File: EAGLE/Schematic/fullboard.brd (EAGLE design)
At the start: 130.2 x 79.7 mm, 77 parts, among them CN1 B4B-XH-A, CN2 B4B-XH-A, IC1 IFX007T, IC2 IFX007T, IC3 IFX007T, IC4 IFX007T, J1 10118193-0001LF, Q1 8MHz ±10ppm Crystal 18pF 80 O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, SW1 TR1-SPST, U1 ATXMEGA128A3U-AU, U2 FT232RL-REEL

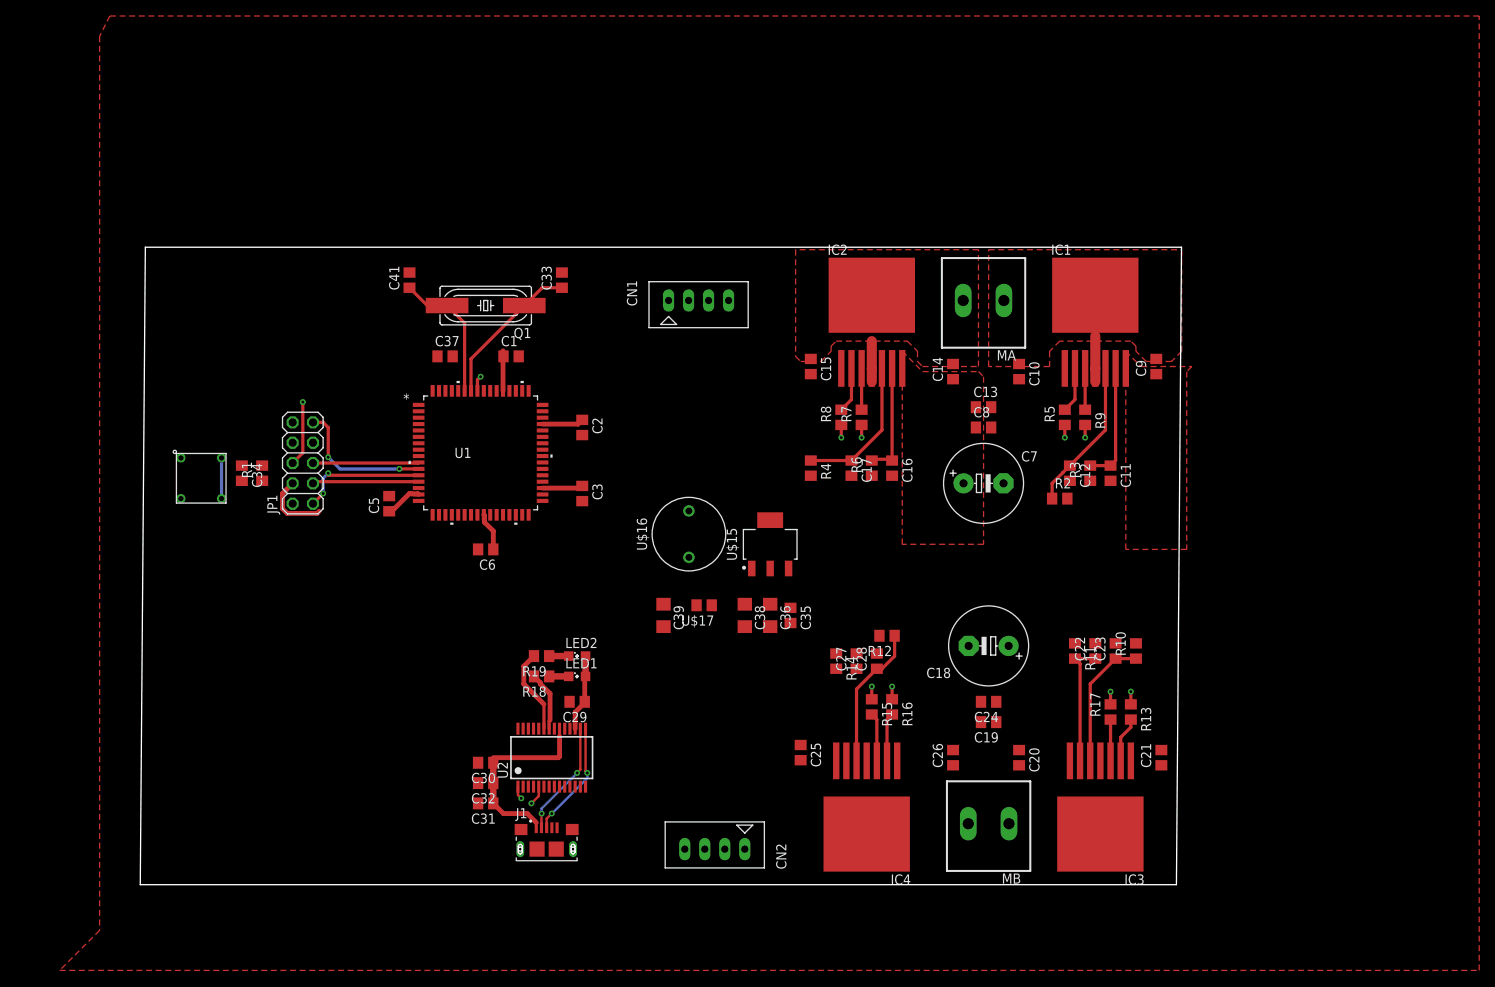
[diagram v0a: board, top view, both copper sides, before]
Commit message: V0.1 of the board
Did some more signal routing, added a connector for the mouse, added a simple 5V regulator circuit
Still need:
* Edge sensor connectors
* Footprint 2x check
* Probably some other things
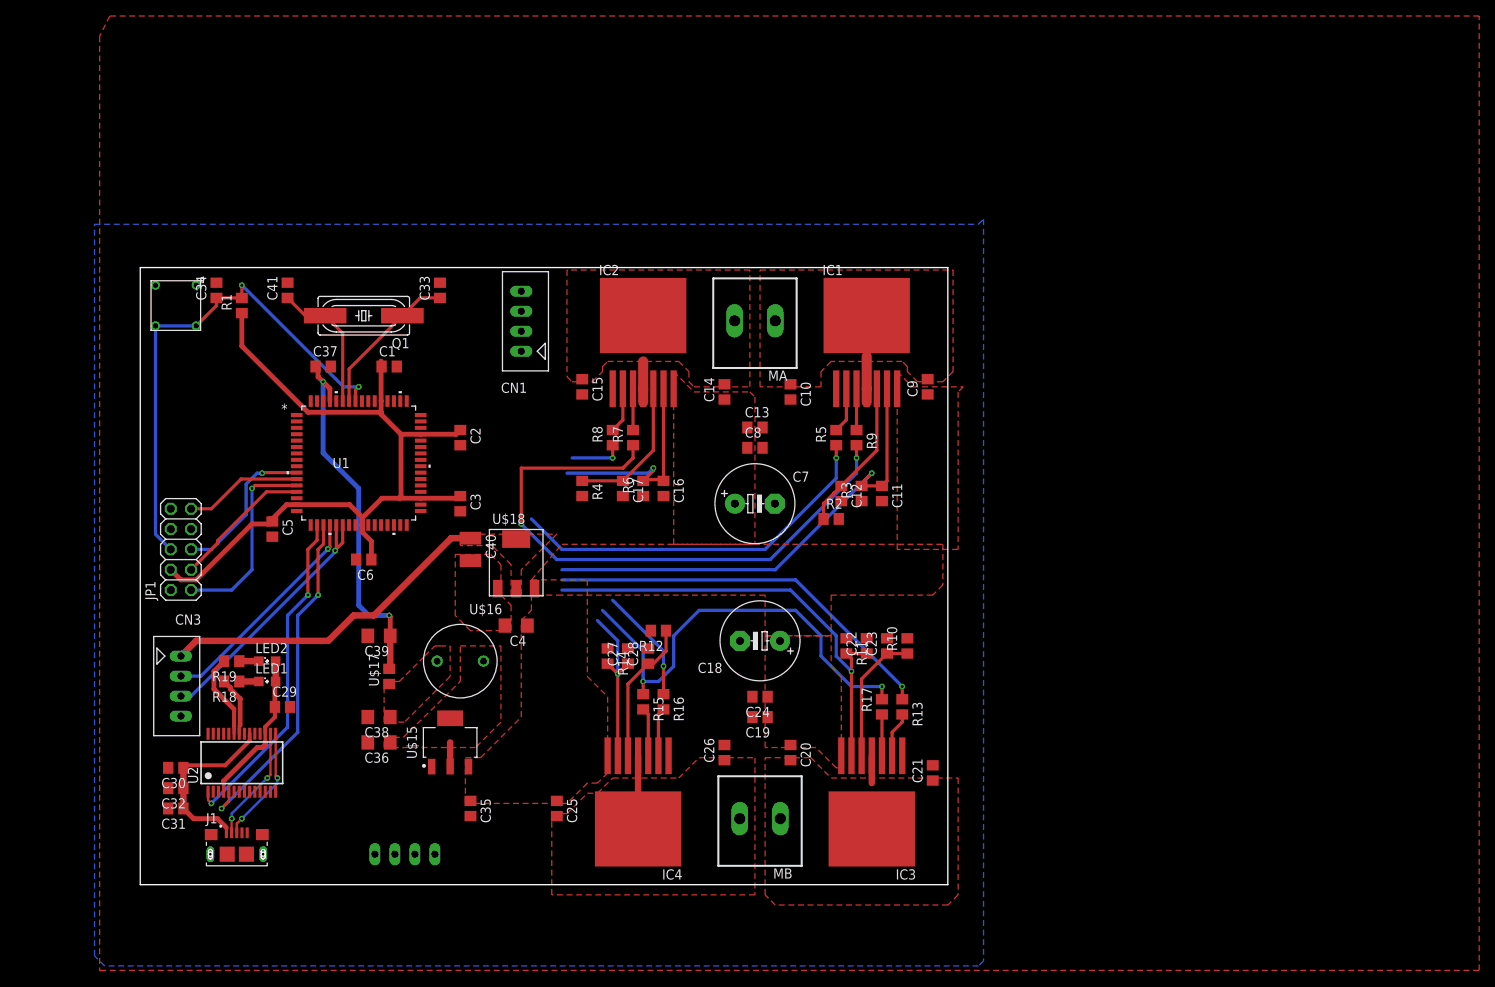
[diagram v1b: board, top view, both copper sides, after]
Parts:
- added C4: 10uF, rcl:C1206
- added C40: 22uF, rcl:C1210
- added CN3: B4B-XH-A, jst:B4B-XH-A
- added U$18: AZ1117IH, SumBot:SOT223
- moved C36 51.4 mm to (29.8, 18.4), turned to 180 degrees
- moved C38 47.5 mm to (29.8, 21.6), turned to 180 degrees
- moved U$15 47.1 mm to (38.7, 18.4)
- moved C35 46.7 mm to (41.3, 10.2)
- moved U$17 40.4 mm to (31.1, 26.7), turned to 90 degrees
- moved C30 38.7 mm to (4.45, 15.2)
- moved C31 38.7 mm to (4.45, 10.2)
- moved C32 38.7 mm to (4.45, 12.7)
- moved CN2 38.7 mm to (36.8, 4.45), flipped to the bottom, turned to 180 degrees
- moved J1 38.7 mm to (12.1, 4.45)
- moved LED1 38.7 mm to (15.9, 26.0)
- moved LED2 38.7 mm to (15.9, 28.6)
- moved R18 38.7 mm to (11.4, 26.0)
- moved R19 38.7 mm to (11.4, 28.6)
- moved U2 38.7 mm to (12.7, 15.9)
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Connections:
- net N$36 renamed VCCIO
- removed net RX_MSE: U1.21
- removed net TX_MSE: U1.22
- new net N$1: C4.2, C40.2, U$18.1
- new net TX/RX_MSE: CN3.3, U1.21, U1.22
- new net USB_PWR: C30.1, C31.1, C32.1, J1.1, U2.20
- net +12V: now also C4.1, U$18.3
- net +5V: now also C40.1, CN3.1, U$18.2, U$18.4; no longer C30.1, C31.1, C32.1, J1.1, U2.20
- net GND: now also CN3.4
- net XCK_MSE: now also CN3.2
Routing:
- net EN_A: track 3.18 -> 74.8 mm
- net +3V3: track 33.4 -> 99.9 mm
- net CS_B: track 15.6 -> 79.0 mm, vias 0 -> 2
- net CS_A: track 29.8 -> 88.8 mm, vias 0 -> 2
- net EN_B: track 3.18 -> 55.4 mm
- net !RESET: track 15.2 -> 64.9 mm
- net FWD_B: track 1.59 -> 49.7 mm
- net AVCC: track 0.00 -> 46.0 mm, vias 0 -> 2
- net FWD_A: track 1.59 -> 47.5 mm
- net TX_FT232: track 2.47 -> 43.2 mm, vias 1 -> 2
- net RX_FT232: track 1.63 -> 41.9 mm, vias 1 -> 2
- net TX/RX_MSE: track 0.00 -> 33.5 mm, vias 0 -> 1
- net XCK_MSE: track 0.00 -> 28.1 mm, vias 0 -> 1
- net USB_PWR: track 0.00 -> 22.2 mm
- net +5V: track 22.6 -> 42.3 mm
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- added copper zone on layer 1, net +3V3
- added copper zone on layer 1, net +5V
- added copper zone on layer 16, net GND
- added copper zone on layer 1, net MB_1
- added copper zone on layer 1, net MB_2
- added copper zone on layer 1, net N$1
- added copper zone on layer 1, net N$8
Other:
- board size 130.2 x 79.7 mm -> 100.9 x 77.1 mm

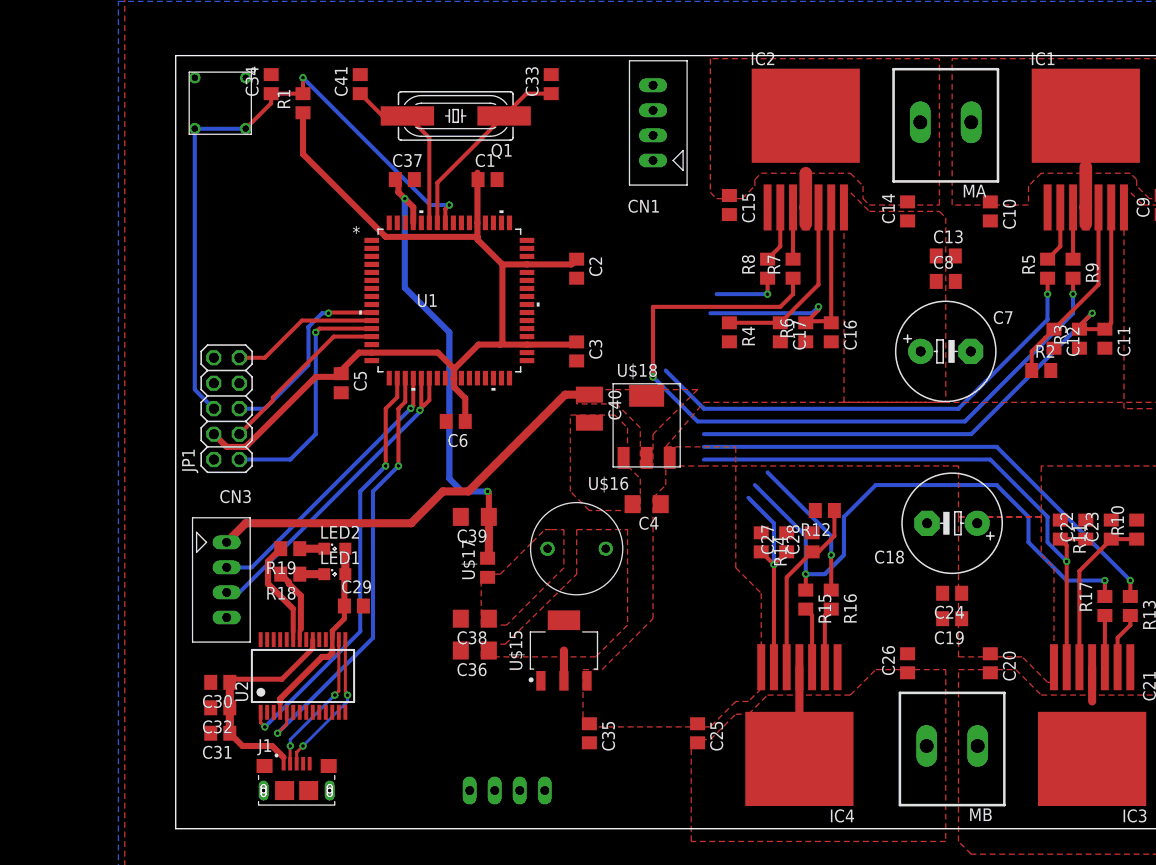
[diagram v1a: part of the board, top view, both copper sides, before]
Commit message: V0.2
Added Edge Detection and reconfigured other pins
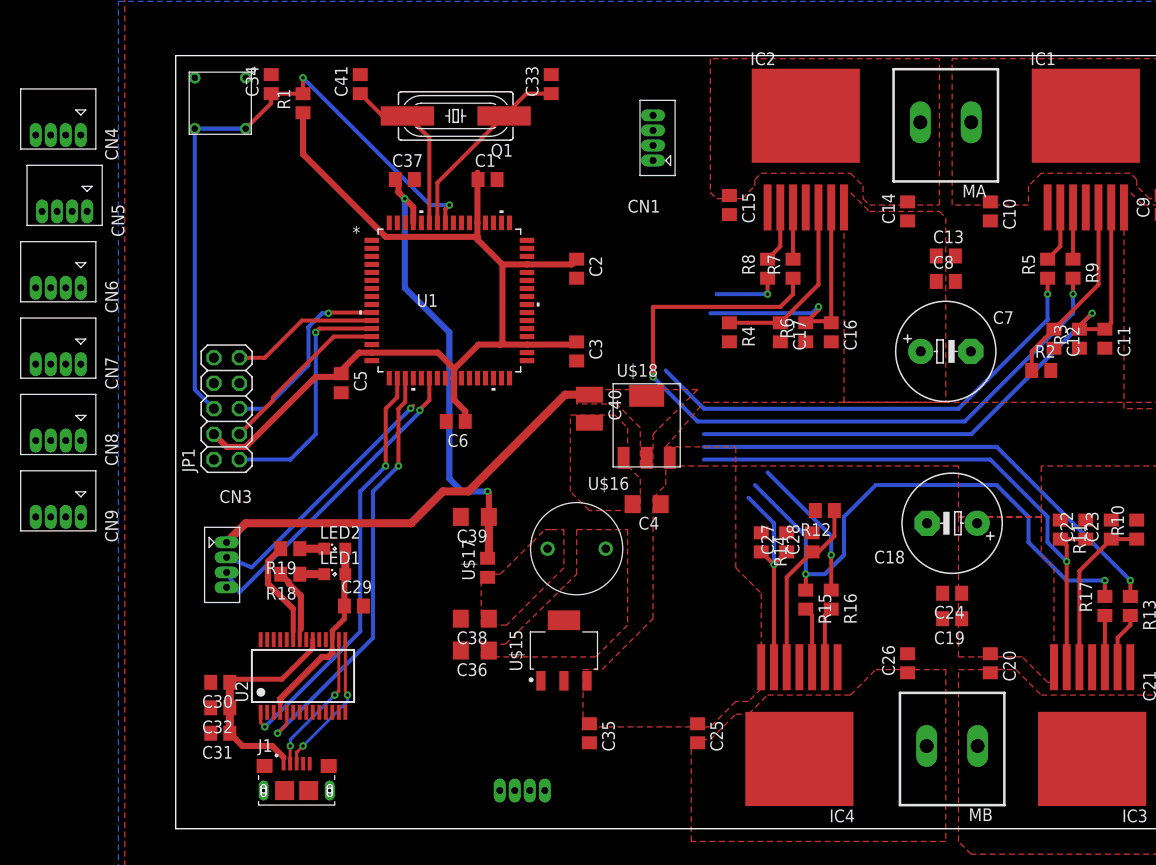
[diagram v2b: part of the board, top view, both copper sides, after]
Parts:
- added CN4, CN5, CN6, CN7, CN8, CN9: S4B-ZR, jst:S4B-ZR
- CN1, CN2, CN3: value B4B-XH-A -> B4B-ZR; device jst:B4B-XH-A -> jst:B4B-ZR
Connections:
- new net EDGE_CTRL: CN4.4, CN5.4, CN6.4, CN7.4, CN8.4, CN9.4, U1.16
- net +3V3: now also CN4.2, CN5.2, CN6.2, CN7.2, CN8.2, CN9.2
- net BCK_A: now also U1.41; no longer U1.27
- net BCK_B: now also U1.38; no longer U1.29
- net EA_A: now also U1.54; no longer U1.50
- net EA_B: now also U1.27; no longer U1.47
- net EB_A: now also U1.55; no longer U1.51
- net EB_B: now also U1.26; no longer U1.48
- net EDGE_A: now also CN4.1, U1.64; no longer U1.62
- net EDGE_B: now also CN5.1, U1.1; no longer U1.63
- net EDGE_C: now also CN6.1, U1.2; no longer U1.64
- net EDGE_D: now also CN7.1, U1.3; no longer U1.1
- net EDGE_E: now also CN8.1, U1.4; no longer U1.2
- net EDGE_F: now also CN9.1, U1.5; no longer U1.3
- net EN_A: now also U1.42; no longer U1.49
- net EN_B: now also U1.37; no longer U1.46
- net FWD_A: now also U1.40; no longer U1.26
- net FWD_B: now also U1.39; no longer U1.28
- net GND: now also CN4.3, CN5.3, CN6.3, CN7.3, CN8.3, CN9.3
- net TX/RX_MSE: now also U1.23; no longer U1.21
- net XCK_MSE: now also U1.21; no longer U1.20
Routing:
- net MA_1: track 5.71 -> 0.00 mm
- net MA_2: track 5.08 -> 0.00 mm
- net MB_2: track 4.69 -> 0.00 mm
- net MB_1: track 3.41 -> 0.00 mm
- net N$8: track 3.02 -> 0.00 mm
- net XCK_MSE: track 28.1 -> 25.5 mm
- net TX/RX_MSE: track 33.5 -> 31.6 mm
